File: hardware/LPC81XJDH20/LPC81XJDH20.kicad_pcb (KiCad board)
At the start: 2 copper layers, 2 parts

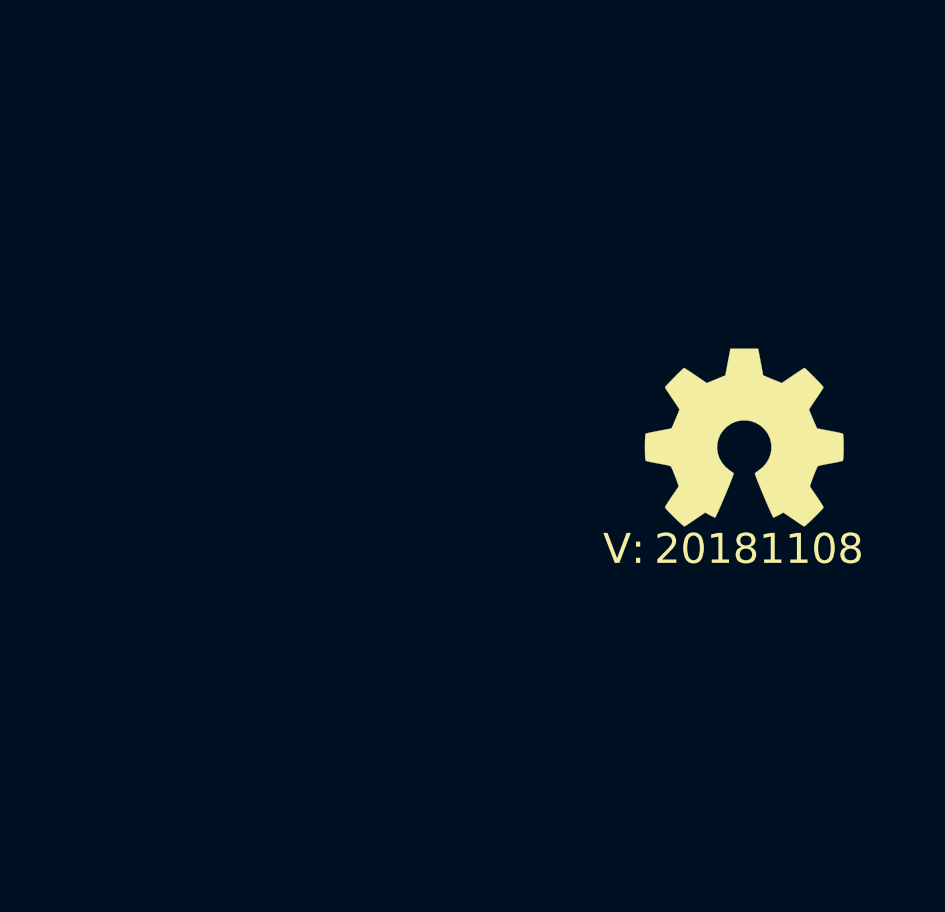
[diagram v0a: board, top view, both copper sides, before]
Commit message: copied over LPC824 to LPC812
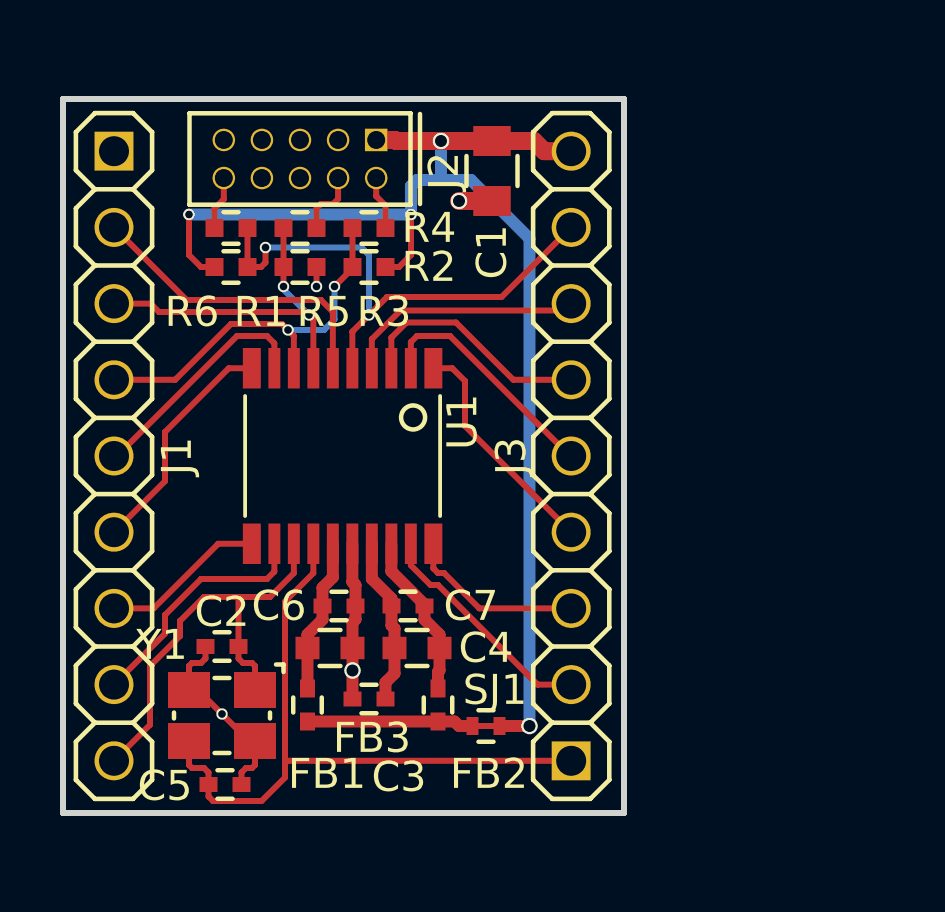
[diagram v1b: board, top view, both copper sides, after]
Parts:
- added C1: 10u, SquantorRcl:C_0805, F.Cu at (139.6, 92.1)
- added C2: 18p, SquantorRcl:C_0402, F.Cu at (130.6, 108.0)
- added C3: 1u, SquantorRcl:C_0603, F.Cu at (134.2, 108.0)
- added C4: 1u, SquantorRcl:C_0603, F.Cu at (137.1, 108.0)
- added C5: 18p, SquantorRcl:C_0402, F.Cu at (130.7, 112.5)
- added C6: 100n, SquantorRcl:C_0402, F.Cu at (134.5, 106.6)
- added C7: 100n, SquantorRcl:C_0402, F.Cu at (136.8, 106.6)
- added FB1: FB, SquantorRcl:C_0402, F.Cu at (133.4, 109.9)
- added FB2: FB, SquantorRcl:C_0402, F.Cu at (137.8, 109.9)
- added FB3: FB, SquantorRcl:C_0402, F.Cu at (135.5, 109.7)
- added J1: Conn_01x09, SquantorConnectors:Header-0254-1X09-H010, F.Cu at (127.0, 101.6)
- added J2: JTAG_2X05, SquantorConnectors:Header-0127-2X05-H006, F.Cu at (133.2, 91.7)
- added J3: Conn_01x09, SquantorConnectors:Header-0254-1X09-H010, F.Cu at (142.2, 101.6)
- added R1: 100K, SquantorRcl:R_0402_hand, F.Cu at (130.9, 95.3)
- added R2: 100k, SquantorRcl:R_0402_hand, F.Cu at (135.5, 95.3)
- added R3: 100k, SquantorRcl:R_0402_hand, F.Cu at (133.2, 95.3)
- added R4: 100, SquantorRcl:R_0402_hand, F.Cu at (135.5, 94.0)
- added R5: 100, SquantorRcl:R_0402_hand, F.Cu at (133.2, 94.0)
- added R6: 100, SquantorRcl:R_0402_hand, F.Cu at (130.9, 94.0)
- added SJ1: SolderJumper_2way_1conn, SquantorSpecial:solder_jumper_2way_conn, F.Cu at (139.4, 110.6)
- added U1: LPC824M201JDH20, SquantorIC:SOT360, F.Cu at (134.6, 101.6)
- added Y1: 12MHz, SquantorCrystal:Crystal_3225_4, F.Cu at (130.6, 110.2)
- N1: moved to B.Cu
- N2: value 20181108 -> 20190121; moved to B.Cu
- moved N2 14.4 mm to (134.5, 104.9)
- moved N1 13.5 mm to (134.5, 101.3), turned to 180 degrees
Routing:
- net VDD: track 0.00 -> 43.1 mm, vias 0 -> 4
- net /PIO0_8: track 0.00 -> 23.0 mm
- net /RESET: track 0.00 -> 18.0 mm, vias 0 -> 2
- net /PIO0_9: track 0.00 -> 14.5 mm
- net VSS: track 0.00 -> 13.5 mm, vias 0 -> 4
- net /PIO0_2: track 0.00 -> 13.0 mm, vias 0 -> 2
- net /PIO0_3: track 0.00 -> 11.7 mm, vias 0 -> 2
- net /PIO0_4: track 0.00 -> 10.3 mm
- net /PIO0_1: track 0.00 -> 8.20 mm
- net /PIO0_12: track 0.00 -> 8.11 mm
- net /PIO0_13: track 0.00 -> 8.02 mm
- net /PIO0_17: track 0.00 -> 7.96 mm
- net /PIO0_11: track 0.00 -> 7.93 mm
- net /PIO0_10: track 0.00 -> 7.82 mm
- net /PIO0_23: track 0.00 -> 7.74 mm
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- added copper zone on B.Cu, net VSS
- added copper zone on F.Cu, net VSS
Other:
- board outline added: 18.7 x 23.8 mm
- rule solder_mask_min_width: 0.15 -> 0.25

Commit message: WIP PCB layout
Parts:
- removed C4: 1u, SquantorRcl:C_0603
- removed C7: 100n, SquantorRcl:C_0402
- removed FB2, FB3: FB, SquantorRcl:C_0402
- removed U1: LPC824M201JDH20, SquantorIC:SOT360
- added U3: LPC812M101JDH20, SquantorIC:SOT360, F.Cu at (134.6, 101.6)
- J1: value Conn_01x09 -> LPC81XJDH20_breakout_left; footprint SquantorConnectors:Header-0254-1X09-H010 -> SquantorConnectorsNamed:LPC81XJDH20_breakout_left; moved to B.Cu
- J3: value Conn_01x09 -> LPC81XJDH20_breakout_right; footprint SquantorConnectors:Header-0254-1X09-H010 -> SquantorConnectorsNamed:LPC81XJDH20_breakout_right; moved to B.Cu
- N2: value 20190121 -> 20190310
- moved SJ1 4.20 mm to (135.2, 110.5)
- moved J2 1.10 mm to (133.2, 90.6)
- moved C1 1.10 mm to (139.6, 91.0)
- moved R1 1.10 mm to (130.9, 94.2)
- moved R2 1.10 mm to (135.5, 94.2)
- moved R3 1.10 mm to (133.2, 94.2)
- moved R4 1.10 mm to (135.5, 92.9)
- moved R5 1.10 mm to (133.2, 92.9)
- moved R6 1.10 mm to (130.9, 92.9)
- turned J3 to 270 degrees
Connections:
- J1 pad 2: /PIO0_4 -> /PIO0_3
- J1 pad 3: /PIO0_3 -> /PIO0_2
- J1 pad 4: /PIO0_2 -> /PIO0_11
- J1 pad 5: /PIO0_11 -> /PIO0_10
- J1 pad 6: /PIO0_10 -> /PIO0_16
- J3 pad 1: /PIO0_8 -> /PIO0_7
- J3 pad 2: /PIO0_0 -> /PIO0_6
- J3 pad 3: /PIO0_14 -> /PIO0_0
- J3 pad 4: /PIO0_23 -> /PIO0_14
- J3 pad 9: VDD -> /PIO0_4
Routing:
- net /PIO0_8: track 23.0 -> 0.00 mm
- net /RESET: track 18.0 -> 0.00 mm, vias 2 -> 0
- net /PIO0_9: track 14.5 -> 0.00 mm
- net /PIO0_2: track 13.0 -> 0.00 mm, vias 2 -> 0
- net /PIO0_3: track 11.7 -> 0.00 mm, vias 2 -> 0
- net /PIO0_4: track 10.3 -> 0.00 mm
- net /PIO0_1: track 8.20 -> 0.00 mm
- net /PIO0_12: track 8.11 -> 0.00 mm
- net /PIO0_13: track 8.02 -> 0.00 mm
- net /PIO0_17: track 7.96 -> 0.00 mm
- net /PIO0_11: track 7.93 -> 0.00 mm
- net /PIO0_10: track 7.82 -> 0.00 mm
- net /PIO0_23: track 7.74 -> 0.00 mm
- net /PIO0_0: track 7.71 -> 0.00 mm
- net /PIO0_14: track 5.97 -> 0.00 mm
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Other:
- board size 18.7 x 23.8 mm -> 18.7 x 26.2 mm

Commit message: layout completed
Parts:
- moved C3 0.41 mm to (134.3, 107.6)
- moved FB1 0.41 mm to (133.6, 109.5)
- moved SJ1 0.41 mm to (135.3, 110.1)
- moved C6 0.41 mm to (134.6, 106.2)
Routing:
- net /PIO0_8: track 0.00 -> 17.5 mm
- net /RESET: track 0.00 -> 16.4 mm, vias 0 -> 2
- net /PIO0_3: track 0.00 -> 13.6 mm
- net /PIO0_2: track 0.00 -> 13.5 mm, vias 0 -> 2
- net /PIO0_7: track 0.00 -> 12.4 mm
- net /PIO0_9: track 0.00 -> 12.0 mm
- net /PIO0_4: track 0.00 -> 10.7 mm
- net /PIO0_6: track 0.00 -> 9.75 mm
- net /PIO0_17: track 0.00 -> 9.07 mm
- net /PIO0_16: track 0.00 -> 8.91 mm
- net /PIO0_13: track 0.00 -> 8.43 mm
- net /PIO0_12: track 0.00 -> 8.39 mm
- net /PIO0_10: track 0.00 -> 7.93 mm
- net /PIO0_11: track 0.00 -> 7.83 mm
- net /PIO0_0: track 0.00 -> 7.22 mm
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
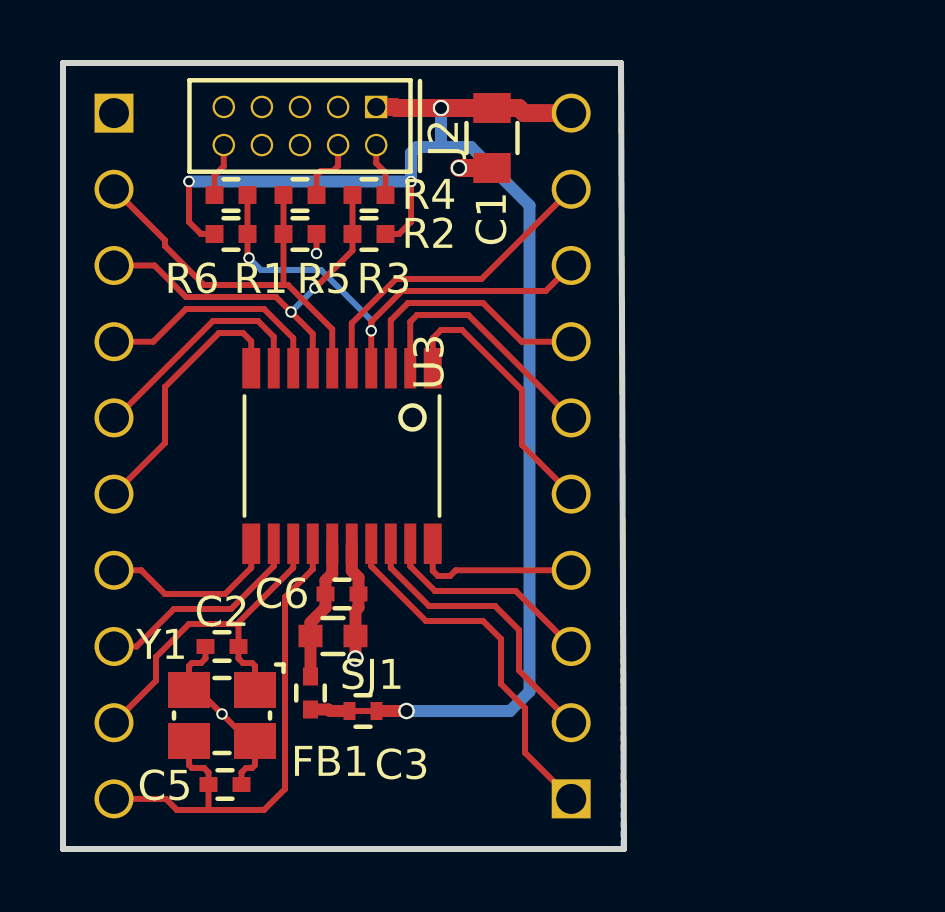
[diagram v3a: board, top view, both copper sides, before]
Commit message: silk layout completed
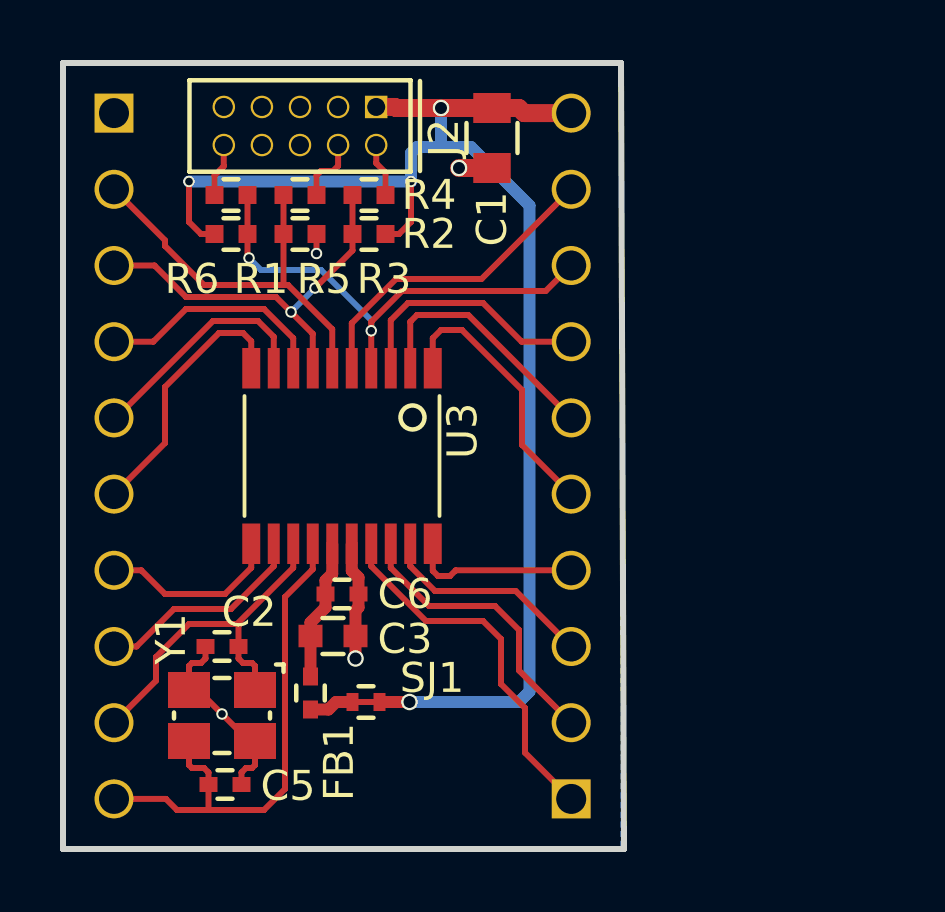
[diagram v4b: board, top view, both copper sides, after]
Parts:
- moved SJ1 0.32 mm to (135.4, 109.8)
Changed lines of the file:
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@@
     (46 B.CrtYd user)
     (47 F.CrtYd user)
-    (48 B.Fab user)
-    (49 F.Fab user)
+    (48 B.Fab user hide)
+    (49 F.Fab user hide)
   )
   (setup
-    (last_trace_width 0.2)
+    (last_trace_width 0.4)
     (user_trace_width 0.1524)
     (user_trace_width 0.2)
@@
     (add_net VSS)
   )
+  (module SquantorSpecial:solder_jumper_2way_conn (layer F.Cu)
+    (at 135.4 109.8 180)
+    (descr "Resistor SMD 0402, reflow soldering, Vishay (see dcrcw.pdf)")
+    (tags "resistor 0402")
+    (attr smd)
+    (fp_text reference SJ1 (at -2.2 0.8) (layer F.SilkS)
+      (effects (font (size 1 1) (thickness 0.15)))
+    )
+    (fp_text value SolderJumper_2way_1conn (at 0 1.8 180) (layer F.Fab) hide
+      (effects (font (size 1 1) (thickness 0.15)))
+    )
+    (fp_line (start -0.5 0.25) (end -0.5 -0.25) (layer F.Fab) (width 0.1))
+    (fp_line (start 0.5 0.25) (end -0.5 0.25) (layer F.Fab) (width 0.1))
+    (fp_line (start 0.5 -0.25) (end 0.5 0.25) (layer F.Fab) (width 0.1))
+    (fp_line (start -0.5 -0.25) (end 0.5 -0.25) (layer F.Fab) (width 0.1))
+    (fp_line (start -0.95 -0.65) (end 0.95 -0.65) (layer F.CrtYd) (width 0.05))
+    (fp_line (start -0.95 0.65) (end 0.95 0.65) (layer F.CrtYd) (width 0.05))
+    (fp_line (start -0.95 -0.65) (end -0.95 0.65) (layer F.CrtYd) (width 0.05))
+    (fp_line (start 0.95 -0.65) (end 0.95 0.65) (layer F.CrtYd) (width 0.05))
+    (fp_line (start 0.25 -0.525) (end -0.25 -0.525) (layer F.SilkS) (width 0.15))
+    (fp_line (start -0.25 0.525) (end 0.25 0.525) (layer F.SilkS) (width 0.15))
+    (fp_line (start -0.3 0) (end 0.3 0) (layer F.Cu) (width 0.2))
+    (pad 1 smd rect (at -0.45 0 180) (size 0.4 0.6) (layers F.Cu F.Paste F.Mask)
+      (net 2 VDD))
+    (pad 2 smd rect (at 0.45 0 180) (size 0.4 0.6) (layers F.Cu F.Paste F.Mask)
+      (net 6 "Net-(FB1-Pad2)"))
+    (model Resistors_SMD.3dshapes/R_0402.wrl
+      (at (xyz 0 0 0))
+      (scale (xyz 1 1 1))
+      (rotate (xyz 0 0 0))
+    )
+  )
   (module SquantorRcl:R_0402_hand (layer F.Cu)
     (at 135.5 94.2 180)
@@
     (at 130.6 110.25 180)
     (attr smd)
-    (fp_text reference Y1 (at 2 2.35 180) (layer F.SilkS)
+    (fp_text reference Y1 (at 1.7 2.55 270) (layer F.SilkS)
       (effects (font (size 1 1) (thickness 0.15)))
     )
@@
     (tags "capacitor 0402")
     (attr smd)
-    (fp_text reference C2 (at 0 1.15) (layer F.SilkS)
+    (fp_text reference C2 (at -0.9 1.15) (layer F.SilkS)
       (effects (font (size 1 1) (thickness 0.15)))
     )
@@
     (tags "capacitor 0603")
     (attr smd)
-    (fp_text reference C3 (at 2.3 4.3) (layer F.SilkS)
+    (fp_text reference C3 (at 2.4 0.1) (layer F.SilkS)
       (effects (font (size 1 1) (thickness 0.15)))
     )
@@
     (tags "capacitor 0402")
     (attr smd)
-    (fp_text reference C5 (at -2 0.05) (layer F.SilkS)
+    (fp_text reference C5 (at 2.1 0.05) (layer F.SilkS)
       (effects (font (size 1 1) (thickness 0.15)))
     )
@@
     (tags "capacitor 0402")
     (attr smd)
-    (fp_text reference C6 (at -2 0) (layer F.SilkS)
+    (fp_text reference C6 (at 2.1 0) (layer F.SilkS)
       (effects (font (size 1 1) (thickness 0.15)))
     )
@@
     (tags "capacitor 0402")
     (attr smd)
-    (fp_text reference FB1 (at 2.3 -0.65 180) (layer F.SilkS)
+    (fp_text reference FB1 (at 2.3 -0.95 270) (layer F.SilkS)
       (effects (font (size 1 1) (thickness 0.15)))
     )
@@
     )
   )
-  (module SquantorSpecial:solder_jumper_2way_conn (layer F.Cu)
-    (at 135.3 110.1 180)
-    (descr "Resistor SMD 0402, reflow soldering, Vishay (see dcrcw.pdf)")
-    (tags "resistor 0402")
-    (attr smd)
-    (fp_text reference SJ1 (at -0.3 1.2) (layer F.SilkS)
-      (effects (font (size 1 1) (thickness 0.15)))
-    )
-    (fp_text value SolderJumper_2way_1conn (at 0 1.8 180) (layer F.Fab) hide
-      (effects (font (size 1 1) (thickness 0.15)))
-    )
-    (fp_line (start -0.5 0.25) (end -0.5 -0.25) (layer F.Fab) (width 0.1))
-    (fp_line (start 0.5 0.25) (end -0.5 0.25) (layer F.Fab) (width 0.1))
-    (fp_line (start 0.5 -0.25) (end 0.5 0.25) (layer F.Fab) (width 0.1))
-    (fp_line (start -0.5 -0.25) (end 0.5 -0.25) (layer F.Fab) (width 0.1))
-    (fp_line (start -0.95 -0.65) (end 0.95 -0.65) (layer F.CrtYd) (width 0.05))
-    (fp_line (start -0.95 0.65) (end 0.95 0.65) (layer F.CrtYd) (width 0.05))
-    (fp_line (start -0.95 -0.65) (end -0.95 0.65) (layer F.CrtYd) (width 0.05))
-    (fp_line (start 0.95 -0.65) (end 0.95 0.65) (layer F.CrtYd) (width 0.05))
-    (fp_line (start 0.25 -0.525) (end -0.25 -0.525) (layer F.SilkS) (width 0.15))
-    (fp_line (start -0.25 0.525) (end 0.25 0.525) (layer F.SilkS) (width 0.15))
-    (fp_line (start -0.3 0) (end 0.3 0) (layer F.Cu) (width 0.2))
-    (pad 1 smd rect (at -0.45 0 180) (size 0.4 0.6) (layers F.Cu F.Paste F.Mask)
-      (net 2 VDD))
-    (pad 2 smd rect (at 0.45 0 180) (size 0.4 0.6) (layers F.Cu F.Paste F.Mask)
-      (net 6 "Net-(FB1-Pad2)"))
-    (model Resistors_SMD.3dshapes/R_0402.wrl
-      (at (xyz 0 0 0))
-      (scale (xyz 1 1 1))
-      (rotate (xyz 0 0 0))
-    )
-  )
   (module SquantorIC:SOT360 (layer F.Cu)
     (at 134.6 101.6 180)
     (descr "<li><b>SOT360</b><hr>\n<ul><li>TSSOP20: plastic thin shrink small outline package; 20 leads; body width 4.4 mm\n<li><u>JEDEC</u>: MO-153\n<li><u>IEC</u>: </ul>")
-    (fp_text reference U3 (at -3.5 2.2 270) (layer F.SilkS)
+    (fp_text reference U3 (at -4.6 -0.1 270) (layer F.SilkS)
       (effects (font (size 1 1) (thickness 0.15)) (justify left bottom))
     )
@@
     (tags "PIN HEADER")
     (attr virtual)
-    (fp_text reference J1 (at -15.24 0 270) (layer B.SilkS)
+    (fp_text reference J1 (at 2.8 -2.1 270) (layer B.SilkS)
       (effects (font (size 1 1) (thickness 0.15)) (justify mirror))
     )
@@
       (effects (font (size 0.6 0.6) (thickness 0.125)) (justify mirror))
     )
-    (fp_text user PIO0_3 (at -8.1 -3 180) (layer B.SilkS)
+    (fp_text user PIO0_3 (at -8.9 -3 180) (layer B.SilkS)
       (effects (font (size 0.6 0.6) (thickness 0.15)) (justify mirror))
     )
@@
     (tags "PIN HEADER")
     (attr virtual)
-    (fp_text reference J3 (at -15.24 0 270) (layer B.SilkS)
+    (fp_text reference J3 (at 2.8 2.24 270) (layer B.SilkS)
       (effects (font (size 1 1) (thickness 0.15)) (justify mirror))
     )
@@
   (segment (start 135.74 89.965) (end 136.365 89.965) (width 0.6) (layer F.Cu) (net 2))
   (segment (start 136.365 89.965) (end 136.4 90) (width 0.6) (layer F.Cu) (net 2))
-  (via (at 136.75 110.1) (size 0.55) (drill 0.4) (layers F.Cu B.Cu) (net 2))
   (via (at 137.9 90) (size 0.55) (drill 0.4) (layers F.Cu B.Cu) (net 2))
   (segment (start 137.9 90.3) (end 137.9 90) (width 0.4) (layer B.Cu) (net 2))
@@
   (segment (start 137.1 91.3) (end 137.9 91.3) (width 0.4) (layer B.Cu) (net 2))
   (segment (start 137.9 90.3) (end 137.9 91.3) (width 0.4) (layer B.Cu) (net 2))
-  (segment (start 136.75 110.1) (end 135.75 110.1) (width 0.4) (layer F.Cu) (net 2))
   (segment (start 139.6 90) (end 140.5 90) (width 0.6) (layer F.Cu) (net 2))
   (segment (start 140.67 90.17) (end 140.5 90) (width 0.6) (layer F.Cu) (net 2))
   (segment (start 142.24 90.17) (end 140.67 90.17) (width 0.6) (layer F.Cu) (net 2))
-  (segment (start 140.85 93.25) (end 140.85 109.45) (width 0.4) (layer B.Cu) (net 2))
-  (segment (start 137.9 91.3) (end 138.9 91.3) (width 0.4) (layer B.Cu) (net 2))
-  (segment (start 140.85 109.45) (end 140.2 110.1) (width 0.4) (layer B.Cu) (net 2))
-  (segment (start 138.9 91.3) (end 140.85 93.25) (width 0.4) (layer B.Cu) (net 2))
-  (segment (start 140.2 110.1) (end 136.75 110.1) (width 0.4) (layer B.Cu) (net 2))
+  (segment (start 136.85 109.8) (end 135.85 109.8) (width 0.4) (layer F.Cu) (net 2))
+  (via (at 136.85 109.8) (size 0.55) (drill 0.4) (layers F.Cu B.Cu) (net 2))
+  (segment (start 138.9 91.3) (end 137.9 91.3) (width 0.4) (layer B.Cu) (net 2))
+  (segment (start 140.85 109.45) (end 140.85 93.25) (width 0.4) (layer B.Cu) (net 2))
+  (segment (start 140.85 93.25) (end 138.9 91.3) (width 0.4) (layer B.Cu) (net 2))
+  (segment (start 136.85 109.8) (end 140.5 109.8) (width 0.4) (layer B.Cu) (net 2))
+  (segment (start 140.5 109.8) (end 140.85 109.45) (width 0.4) (layer B.Cu) (net 2))
   (segment (start 128.4 108.3) (end 128.4 109.09) (width 0.2) (layer F.Cu) (net 3))
   (segment (start 129.5 107.2) (end 128.4 108.3) (width 0.2) (layer F.Cu) (net 3))
@@
   (segment (start 129.5 111.9) (end 129.5 111.1) (width 0.2) (layer F.Cu) (net 5))
   (segment (start 129.6 112) (end 129.5 111.9) (width 0.2) (layer F.Cu) (net 5))
-  (segment (start 134.2 110.1) (end 134.85 110.1) (width 0.4) (layer F.Cu) (net 6))
   (segment (start 133.55 110.05) (end 134.15 110.05) (width 0.4) (layer F.Cu) (net 6))
-  (segment (start 134.15 110.05) (end 134.2 110.1) (width 0.4) (layer F.Cu) (net 6))
+  (segment (start 134.4 109.8) (end 134.95 109.8) (width 0.4) (layer F.Cu) (net 6))
+  (segment (start 134.15 110.05) (end 134.4 109.8) (width 0.4) (layer F.Cu) (net 6))
   (segment (start 139.25 95.7) (end 142.24 92.71) (width 0.2) (layer F.Cu) (net 7))
   (segment (start 136.4 95.7) (end 139.25 95.7) (width 0.2) (layer F.Cu) (net 7))
